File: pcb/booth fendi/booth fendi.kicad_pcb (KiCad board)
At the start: 2 copper layers, 144.8 x 99.1 mm, 8 parts, among them J1 Conn_01x01_Female, J2 Conn_01x03_Female, J3 Conn_01x05_Female, J4 Conn_01x03_Female, J5 Conn_01x07_Female, J6 Conn_01x05_Female, J7 Conn_01x03

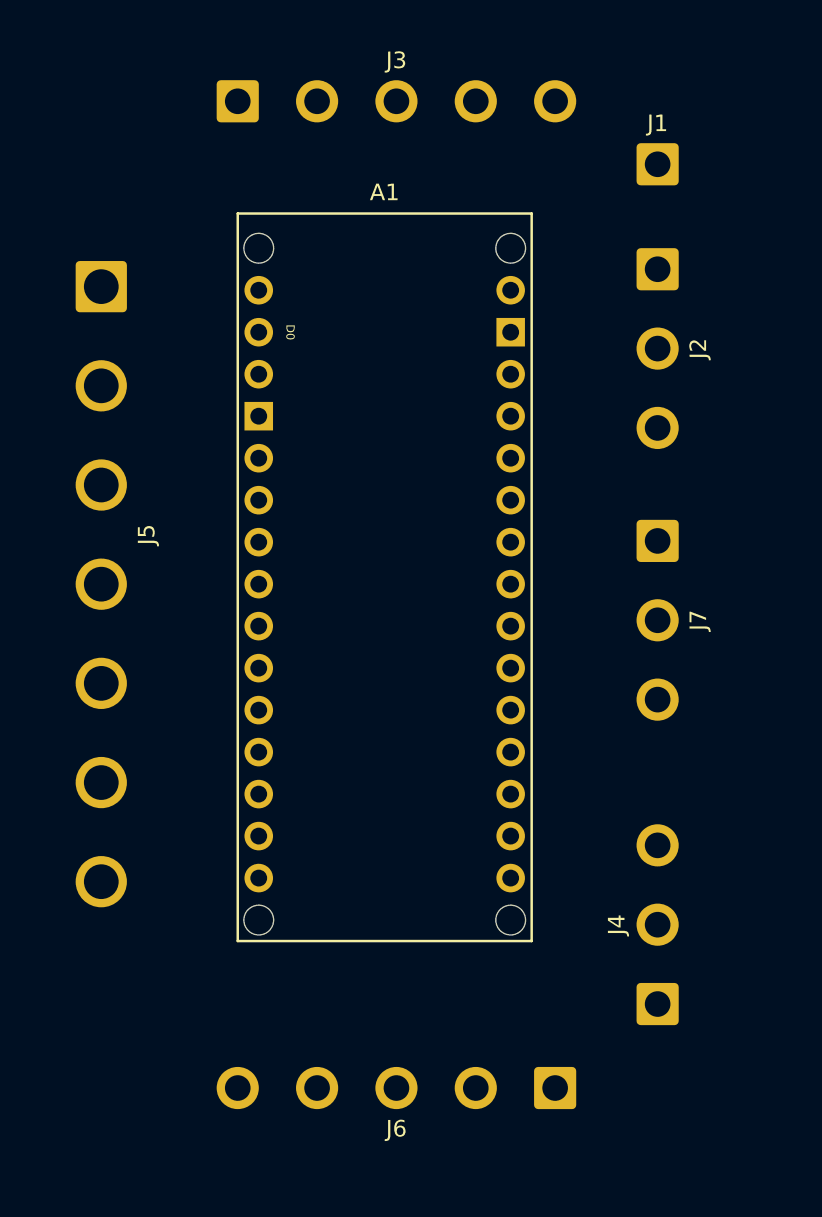
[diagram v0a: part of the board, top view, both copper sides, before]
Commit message: Tracing GND
Traced GND on the PCB
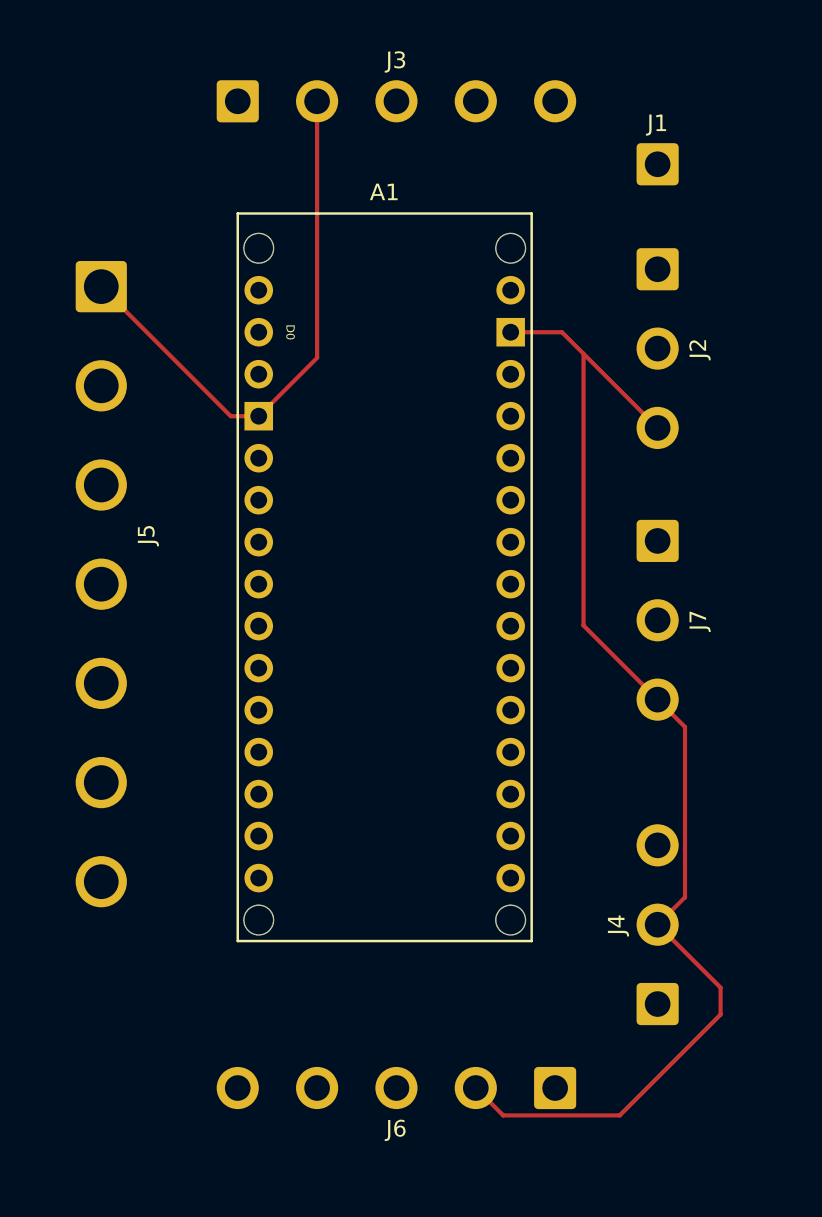
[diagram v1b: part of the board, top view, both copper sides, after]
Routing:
- net GND: track 0.00 -> 107.4 mm

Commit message: traced no silkscreen
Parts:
- removed J1: Conn_01x01_Female, Connector_Wire:SolderWire-0.75sqmm_1x01_D1.25mm_OD2.3mm
- moved J3 44.9 mm to (121.9, 97.8), turned to 90 degrees
- moved J6 43.8 mm to (181.6, 78.6), turned to -90 degrees
- moved J4 41.3 mm to (176.5, 72.4), turned to 180 degrees
- moved J2 37.0 mm to (132.1, 72.4), turned to 0 degrees
- moved J5 36.5 mm to (133.1, 106.0), turned to 0 degrees
- moved A1 28.7 mm to (172.7, 88.9), turned to 90 degrees
- moved J7 24.0 mm to (148.5, 72.4), turned to 0 degrees
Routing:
- net GND: track 107.4 -> 0.00 mm
- net +3V3: track 1.12 -> 104.0 mm
- net SDA: track 0.00 -> 67.4 mm
- net SCL: track 0.00 -> 66.3 mm
- net ETH-SCLK: track 0.00 -> 43.1 mm, vias 0 -> 1
- net TTL-DATA: track 0.00 -> 42.5 mm, vias 0 -> 1
- net SB-X: track 0.00 -> 38.2 mm
- net ETH-RST: track 0.00 -> 34.6 mm
- net SA-X: track 0.00 -> 32.8 mm
- net +5V: track 0.00 -> 28.2 mm
- net ETH-SCS: track 0.00 -> 22.6 mm
- net ETH-MOSI: track 0.00 -> 19.9 mm
- net +12V: track 0.00 -> 19.6 mm
- net ETH-MISO: track 0.00 -> 15.7 mm
- added copper zone on F.Cu, net GND
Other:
- board size 144.8 x 99.1 mm -> 71.1 x 45.7 mm

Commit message: Retraced, need the silkscreen
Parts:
- moved J2 5.24 mm to (137.2, 73.7), turned to 180 degrees
- moved J4 4.02 mm to (172.7, 73.7)
- moved J7 4.02 mm to (144.7, 73.7)
- moved J5 3.51 mm to (134.6, 102.9)
- moved J3 1.30 mm to (123.2, 98.0)
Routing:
- net +12V: track 19.6 -> 7.55 mm
- net +3V3: track 104.0 -> 98.0 mm
- net ETH-MOSI: track 19.9 -> 16.4 mm
- net TTL-DATA: track 42.5 -> 39.6 mm
- net ETH-SCS: track 22.6 -> 19.8 mm
- net ETH-SCLK: track 43.1 -> 40.3 mm
- net ETH-MISO: track 15.7 -> 12.9 mm
- net SDA: track 67.4 -> 66.2 mm
- net SCL: track 66.3 -> 65.1 mm
- net ETH-RST: track 34.6 -> 35.6 mm
- net SA-X: track 32.8 -> 33.7 mm
- added copper zone on B.Cu, net GND
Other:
- board size 71.1 x 45.7 mm -> 66 x 35.6 mm
- board text added: "@luziato"

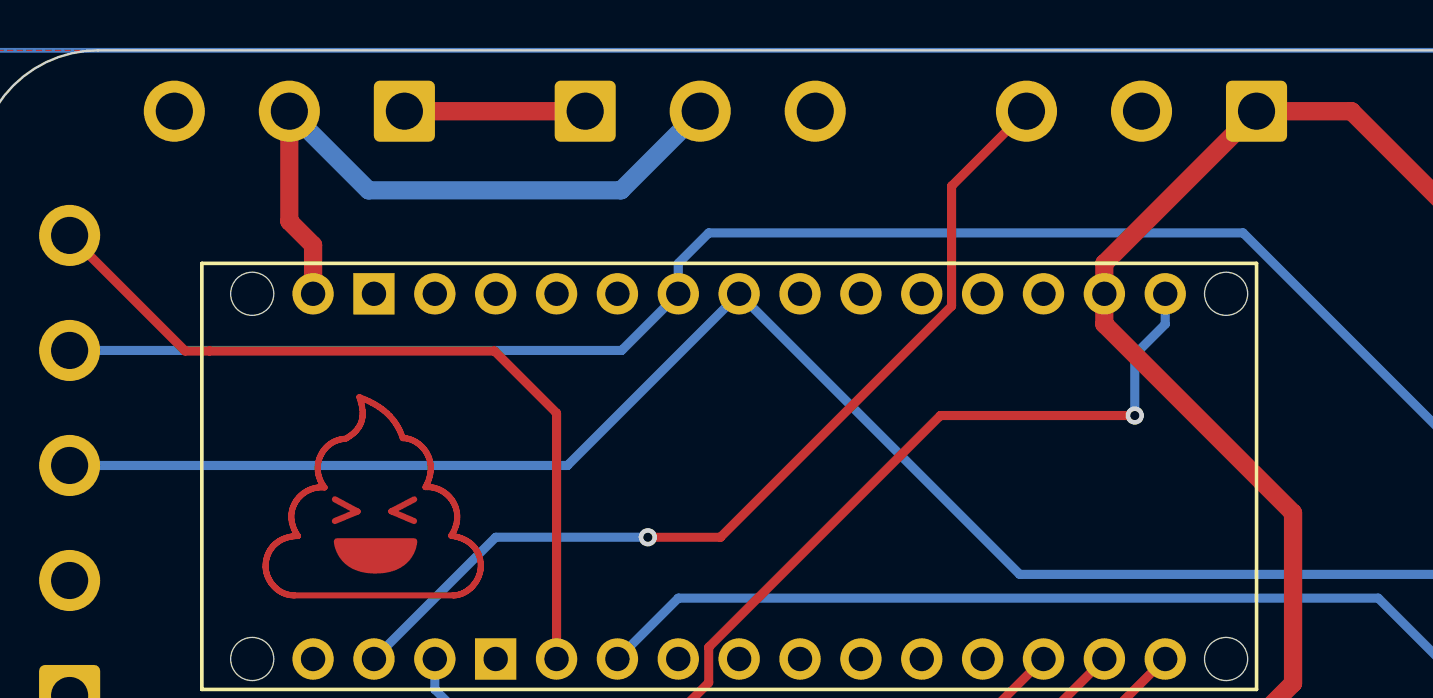
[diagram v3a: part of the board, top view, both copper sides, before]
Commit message: Completed, To be reviewed DRC errors
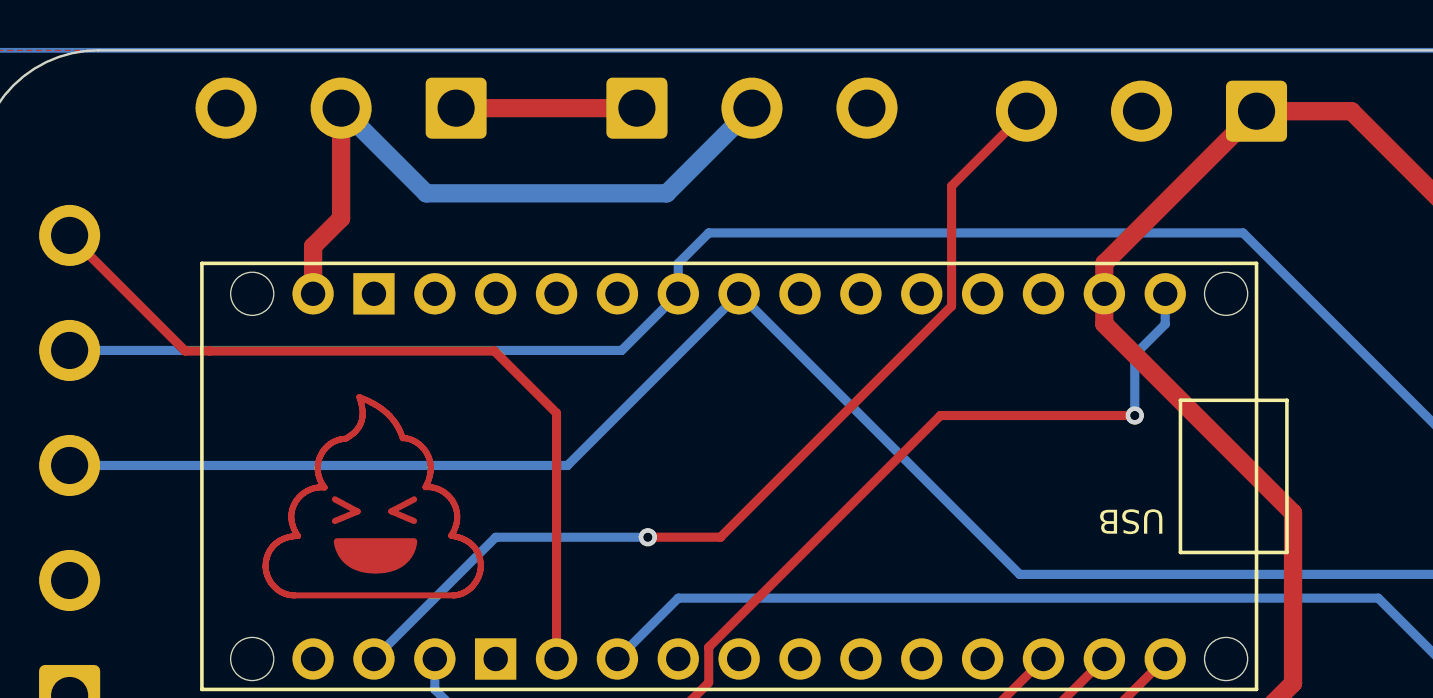
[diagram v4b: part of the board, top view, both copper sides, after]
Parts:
- moved J2 2.16 mm to (139.3, 73.5)
- moved J7 2.16 mm to (146.9, 73.5)
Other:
- board text added: "12V"
- board text added: "3V3"
- board text added: "5V"
- board text added: "ETH"
- board text added: "GND"
- board text added: "MISO"
- board text added: "MOSI"
- board text added: "RST"
- board text added: "SCL"
- board text added: "SCLK"
- board text added: "SCS"
- board text added: "SDA"
- board text added: "SensA"
- board text added: "SensB"
- board text added: "TTL"
- board text added: "TTL-D"
- board text added: "USB"
- board text added: "sAx"
- board text added: "sBx"

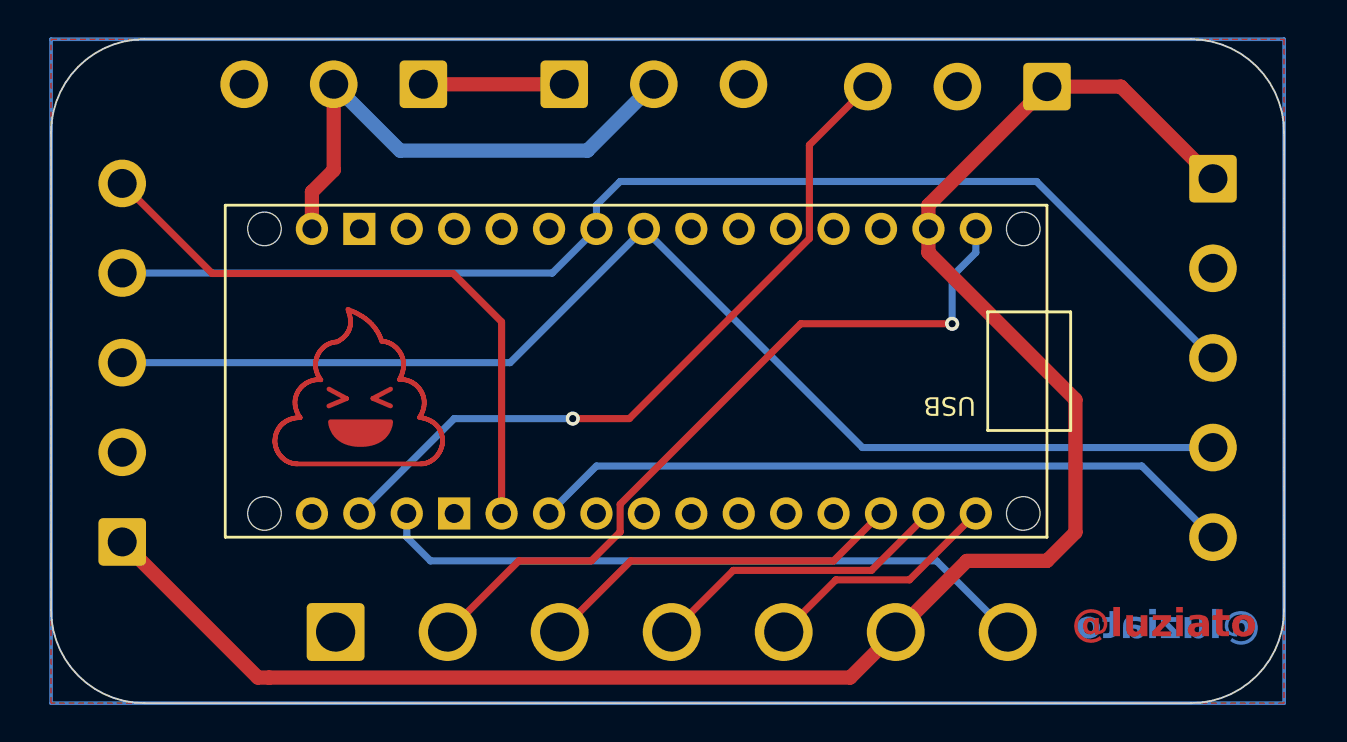
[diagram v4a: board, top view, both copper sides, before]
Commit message: To be reviewed drc errors
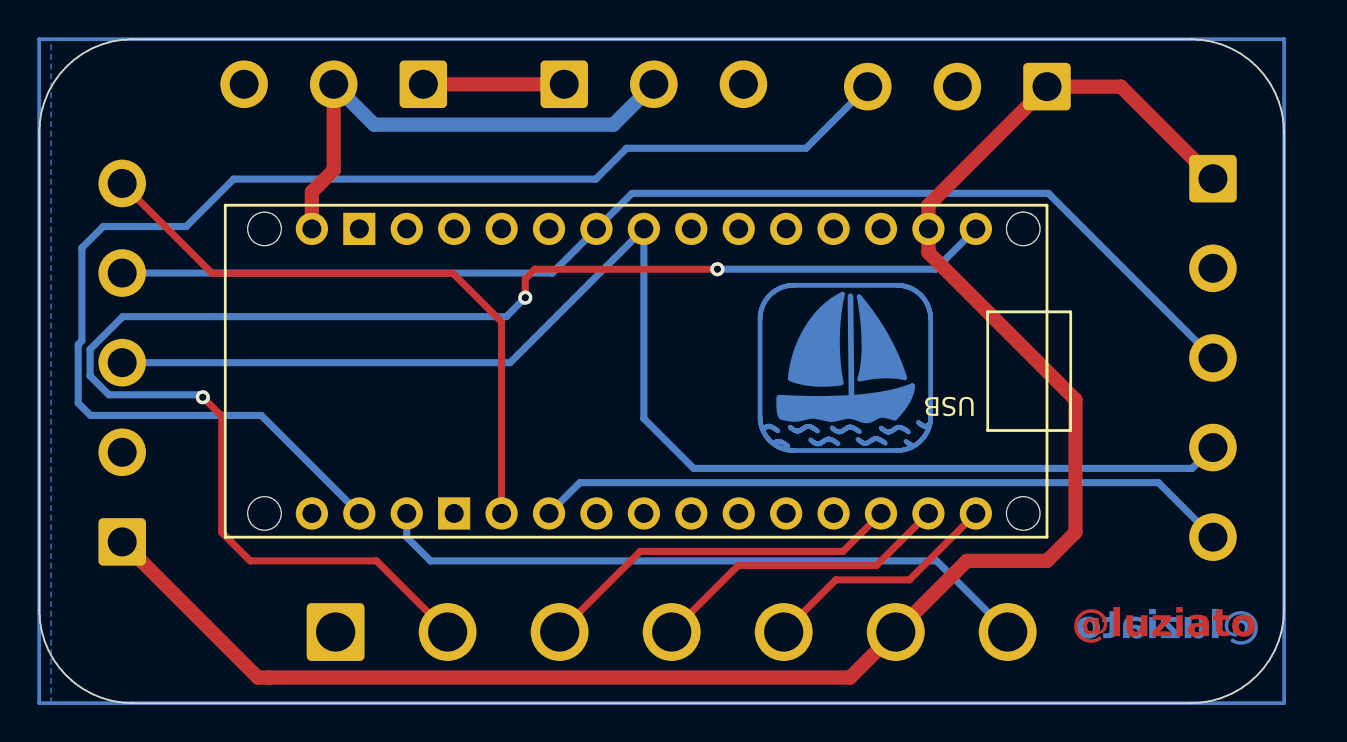
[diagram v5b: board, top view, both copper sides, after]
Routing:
- net ETH-SCLK: track 40.3 -> 80.6 mm, vias 1 -> 3
- net TTL-DATA: track 39.6 -> 71.6 mm, vias 1 -> 0
- net SDA: track 66.2 -> 73.1 mm
- net SCL: track 65.1 -> 63.8 mm
- net +5V: track 28.3 -> 27.2 mm
- net SB-X: track 38.2 -> 37.5 mm
- removed copper zone on F.Cu, net GND
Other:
- board size 66 x 35.6 mm -> 66.7 x 35.6 mm
